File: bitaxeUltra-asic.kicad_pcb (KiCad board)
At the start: 4 copper layers, 56.5 x 99.8 mm, 137 parts, among them J1 54-00164, J2 Conn_01x02, J3 Conn_01x05, J4 Conn_01x04, J5 TC2030-IDC, J7 Conn_01x02, J8 USB_C_Receptacle_USB2.0, J9 Conn_01x04, Q1 CSD17311Q5, Q2 CSD17311Q5, Q4 2N7002K, SW1 GT-TC029B-H025-L1N, SW2 GT-TC029B-H025-L1N, U1 25MHz, U10 DS4432U+, U11 RT9080-33GJ5, U12 ESP32-S3-WROOM-1, U14 BM1366_mode1, U2 TXB0104RGYR, U5 MCP1824T-1802E, U6 MCP1824T-0802E, U7 EMC2101, U8 INA260, U9 TPS40305, Y1 32.768kHz

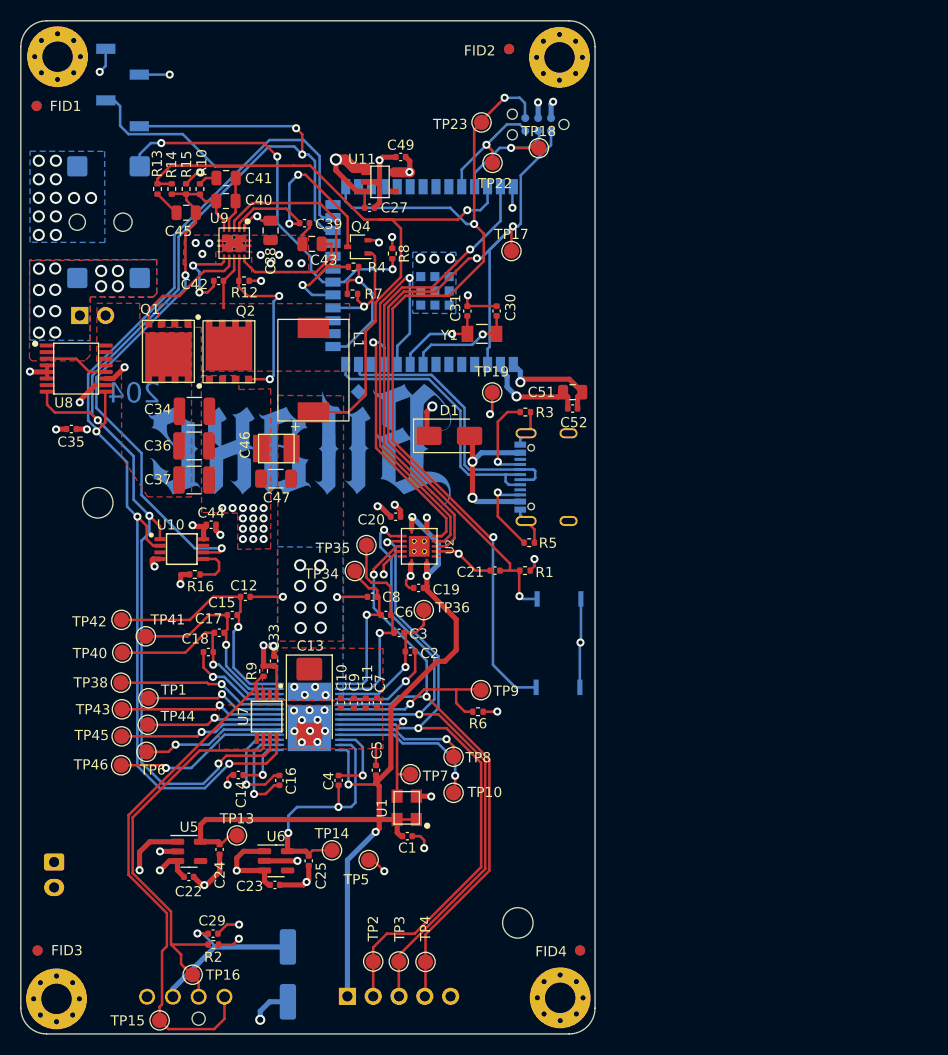
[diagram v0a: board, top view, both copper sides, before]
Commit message: routing for ASIC board
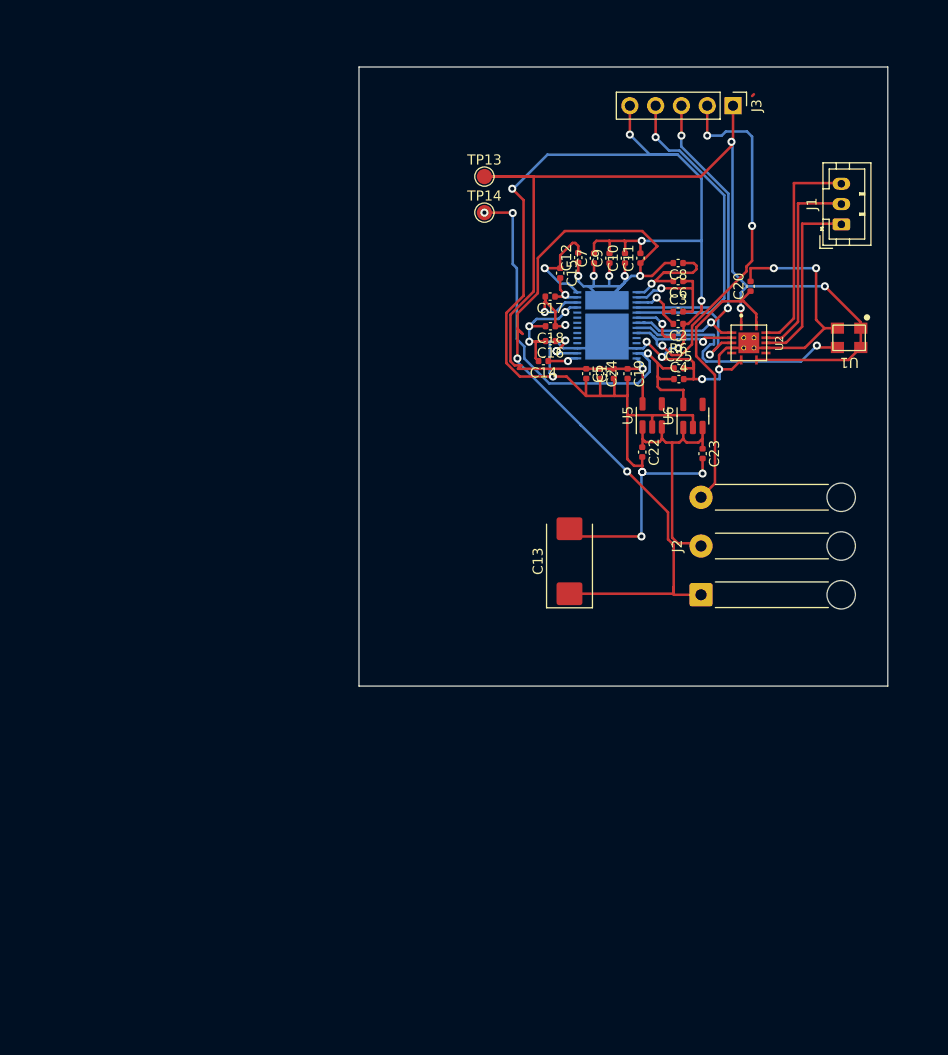
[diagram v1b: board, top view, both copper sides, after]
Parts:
- removed C21, C27, C35, C44, C49: 1uF, Capacitor_SMD:C_0402_1005Metric
- removed C28: 220uF, Capacitor_SMD:CP_Elec_6.3x7.7
- removed C29, C33, C42, C52: 0.1uF, Capacitor_SMD:C_0402_1005Metric
- removed C30, C31: 6.8pF, Capacitor_SMD:C_0402_1005Metric
- removed C34, C36, C37: 47uF, Capacitor_SMD:C_1210_3225Metric
- removed C38: 1uF, Capacitor_SMD:C_0805_2012Metric
- removed C39: 3.3nF, Capacitor_SMD:C_0402_1005Metric
- removed C40: 180pF, Capacitor_SMD:C_0805_2012Metric
- removed C41: 1.5nF, Capacitor_SMD:C_0805_2012Metric
- removed C43, C51: 10uF, Capacitor_SMD:C_0805_2012Metric
- removed C45: 470pF, Capacitor_SMD:C_0805_2012Metric
- removed C46: 220uF, bitaxe:CAP_2R5TPE220MAFB
- removed C47: 100uF, Capacitor_SMD:C_1206_3216Metric
- removed D1: SS310, Diode_SMD:D_SMA
- removed FID1, FID2, FID3, FID4, FID5, FID6, FID7, FID8: Fiducial, Fiducial:Fiducial_1mm_Mask2mm
- removed G***: LOGO, bitaxe:logo
- removed G***: LOGO, bitaxe:logo-fcu
- removed H10, H7, H8, H9: MountingHole_Pad, MountingHole:MountingHole_3mm_Pad_Via
- removed H5, H6: MountingHole, MountingHole:MountingHole_3.5mm
- removed J4: Conn_01x04, bitaxe:470531000
- removed J5: TC2030-IDC, bitaxe:Tag-Connect_TC2030-IDC-NL_2x03_P1.27mm_Vertical
- removed J7: Conn_01x02, Connector_PinHeader_2.54mm:PinHeader_1x02_P2.54mm_Vertical
- removed J8: USB_C_Receptacle_USB2.0, Connector_USB:USB_C_Receptacle_GCT_USB4105-xx-A_16P_TopMnt_Horizontal
- removed J9: Conn_01x04, Connector_PinSocket_2.54mm:PinSocket_1x04_P2.54mm_Vertical_SMD_Pin1Right
- removed L1: 150nH, bitaxe:FP1005R1-R15-R
- removed Q1, Q2: CSD17311Q5, bitaxe:CSD17311Q5
- removed Q4: 2N7002K, Package_TO_SOT_SMD:SOT-323_SC-70
- removed R1, R4, R7, R9: 10k, Resistor_SMD:R_0402_1005Metric
- removed R10: 3.83k, Resistor_SMD:R_0402_1005Metric
- removed R12: 4.12k, Resistor_SMD:R_0402_1005Metric
- removed R13: 1.33k, Resistor_SMD:R_0402_1005Metric
- removed R14: 4.99k, Resistor_SMD:R_0402_1005Metric
- removed R15: 3.32k, Resistor_SMD:R_0402_1005Metric
- removed R16: 80.6k, Resistor_SMD:R_0402_1005Metric
- removed R2: 5.6k, Resistor_SMD:R_0402_1005Metric
- removed R3, R5: 5.1k, Resistor_SMD:R_0402_1005Metric
- removed R8: 1M, Resistor_SMD:R_0402_1005Metric
- removed SW1, SW2: GT-TC029B-H025-L1N, bitaxe:SW_CS1213AGF260_CRS
- removed TP1, TP10, TP15, TP16, TP17, TP18, TP19, TP2, TP22, TP23, TP3, TP34, TP35, TP36, TP38, TP4, TP40, TP41, TP42, TP43, TP44, TP45, TP46, TP5, TP6, TP7, TP8, TP9: TestPoint, TestPoint:TestPoint_Pad_D1.5mm
- removed U10: DS4432U+, Package_SO:TSSOP-8_3x3mm_P0.65mm
- removed U11: RT9080-33GJ5, bitaxe:RT9080-33GJ5
- removed U12: ESP32-S3-WROOM-1, bitaxe:ESP32-S3-WROOM-1
- removed U3: ~, bitaxe:polarity
- removed U7: EMC2101, Package_SO:TSSOP-8_3x3mm_P0.65mm
- removed U8: INA260, Package_SO:TSSOP-16_4.4x5mm_P0.65mm
- removed U9: TPS40305, bitaxe:TPS40305
- removed Y1: 32.768kHz, bitaxe:SC32S-7PF20PPM
- J1: value 54-00164 -> Conn_01x03_Pin; footprint bitaxe:BarrelJack_Wuerth_694106106102_2.0x5.5mm -> Connector_JST:JST_PH_B3B-PH-K_1x03_P2.00mm_Vertical; moved to F.Cu
- J2: value Conn_01x02 -> Conn_01x03_Pin; footprint bitaxe:JST_XH_B2B-XH-A_1x02_P2.50mm_Vertical -> Connector_Wire:SolderWire-0.5sqmm_1x03_P4.8mm_D0.9mm_OD2.3mm_Relief; moved to F.Cu
- J3: moved to F.Cu
- moved J3 95.6 mm to (147.3, 55.9)
- moved J1 72.2 mm to (158.0, 67.6)
- moved TP13 69.3 mm to (122.8, 62.9)
- moved J2 68.9 mm to (144.2, 104.0), turned to 90 degrees
- moved TP14 64.6 mm to (122.8, 66.4)
- moved U1 63.6 mm to (158.8, 78.7), turned to 180 degrees
- moved U5 62.6 mm to (139.4, 86.4), turned to 90 degrees
- moved C22 61.2 mm to (138.4, 90.0), turned to -90 degrees
- moved C25 60.7 mm to (142.0, 81.7), turned to 0 degrees
- moved U6 60.0 mm to (143.4, 86.4), turned to 90 degrees
- moved C24 60.0 mm to (134.2, 82.3)
- moved C23 59.8 mm to (144.3, 90.1), turned to -90 degrees
- moved C10 52.0 mm to (136.7, 70.9), turned to 90 degrees
- moved C4 51.8 mm to (142.0, 82.8), turned to 0 degrees
- moved C11 51.5 mm to (138.2, 70.9), turned to 90 degrees
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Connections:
- J1 pad 1: /Power/VIN -> /RST
- J1 pad 2: GND -> /TX
- J1 pad 3: /PLUG_SENSE -> /RX
- J2 pad 1: GND -> /VDD
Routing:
- net /5V: track 217.6 -> 26.0 mm, vias 7 -> 0
- net /SDA: track 128.0 -> 0.00 mm, vias 5 -> 0
- net /SCL: track 126.5 -> 0.00 mm, vias 3 -> 0
- net /ESP32/IO0: track 92.0 -> 0.00 mm, vias 3 -> 0
- net GND: track 148.3 -> 231.6 mm, vias 83 -> 19
- net /ESP32/EN: track 81.0 -> 0.00 mm, vias 3 -> 0
- net /Power/OUT0: track 55.9 -> 0.00 mm, vias 2 -> 0
- net /Fan/FAN_PWM: track 51.9 -> 0.00 mm
- net /3V3: track 74.3 -> 28.1 mm, vias 15 -> 0
- net /Fan/FAN_TACH: track 40.6 -> 0.00 mm
- net /PLUG_SENSE: track 38.4 -> 0.00 mm, vias 3 -> 0
- net /BM1366/RO: track 66.2 -> 34.8 mm, vias 2 -> 3
- net /RST: track 46.2 -> 18.2 mm, vias 1 -> 0
- net Net-(U12-GPIO20/U1CTS/ADC2_CH9/CLK_OUT1/USB_D+): track 27.8 -> 0.00 mm
- net Net-(U12-GPIO19/U1RTS/ADC2_CH8/CLK_OUT2/USB_D-): track 27.5 -> 0.00 mm
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- removed copper zone on In2.Cu, net /3V3
- removed copper zone on F.Cu, net /5V
- removed copper zone on F.Cu, net /Power/SW
- removed copper zone on B.Cu, net /Power/VIN
- removed copper zone on F.Cu, net /Power/VIN
- removed copper zone on B.Cu, net /VDD
- removed copper zone on F.Cu, net /VDD
- removed copper zone on B.Cu, net GND
- removed copper zone on F.Cu, net GND
- removed copper zone on In1.Cu, net GND
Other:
- board size 56.5 x 99.8 mm -> 52.1 x 61 mm
- board text removed: "/ 21M"
- board text removed: "1V8"
- board text removed: "204"
- board text removed: "5V"
- board text removed: "GND"
- board text removed: "PWM"
- board text removed: "RST"
- board text removed: "RXI"
- board text removed: "TAC"
- board text removed: "TXO"
- board text removed: "∞"

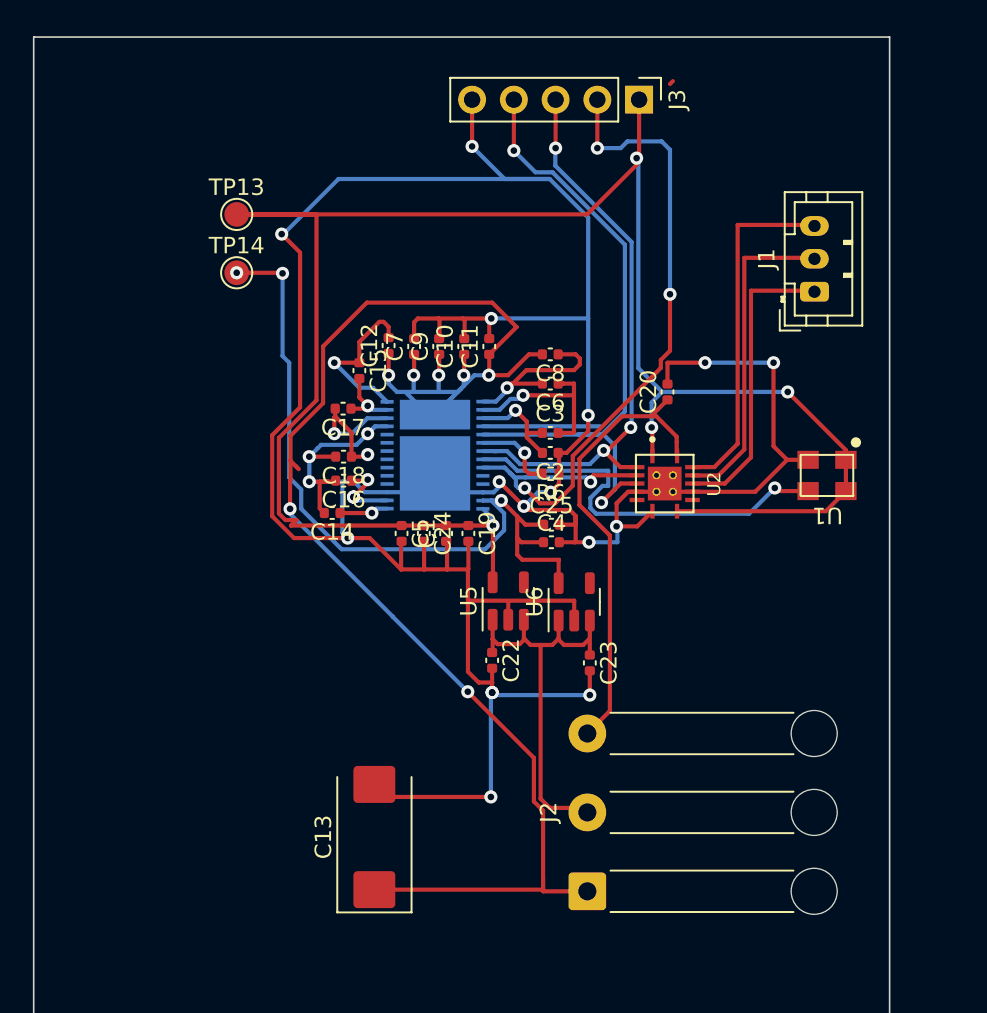
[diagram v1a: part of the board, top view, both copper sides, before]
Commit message: revert  to 4 layer-board routing
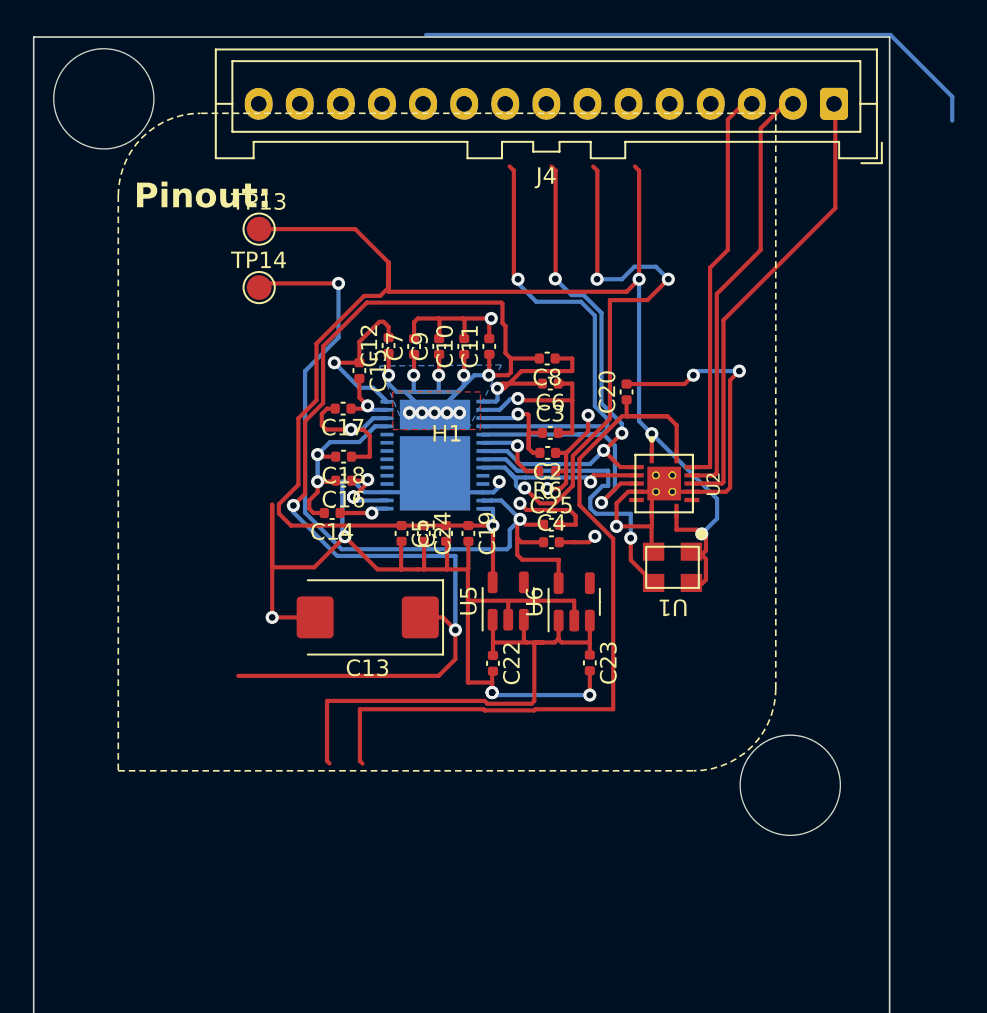
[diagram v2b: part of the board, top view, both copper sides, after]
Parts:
- removed J1: Conn_01x03_Pin, Connector_JST:JST_PH_B3B-PH-K_1x03_P2.00mm_Vertical
- removed J2: Conn_01x03_Pin, Connector_Wire:SolderWire-0.5sqmm_1x03_P4.8mm_D0.9mm_OD2.3mm_Relief
- removed J3: Conn_01x05, Connector_PinHeader_2.54mm:PinHeader_1x05_P2.54mm_Vertical
- added H1: MountingHole, bitaxe:heatsink_mount_bridge, F.Cu at (135.6, 76.7)
- added J4: Conn_01x15, Connector_JST:JST_XA_B15B-XASK-1_1x15_P2.50mm_Vertical, F.Cu at (159.2, 56.1)
- moved C13 13.4 mm to (130.8, 87.4), turned to 180 degrees
- moved U1 10.9 mm to (149.4, 84.3)
- moved C20 2.49 mm to (146.6, 73.7)
- moved TP14 1.64 mm to (124.2, 67.3)
- moved TP13 1.63 mm to (124.2, 63.8)
- moved C8 0.31 mm to (141.7, 71.6)
- moved R6 0.26 mm to (141.7, 78.5)
- moved C22 0.19 mm to (138.4, 90.2)
- moved C2 0.16 mm to (141.8, 77.4)
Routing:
- net GND: track 231.6 -> 157.8 mm, vias 19 -> 16
- net (no net): track 0.00 -> 35.0 mm
- net /BM1366/1V8: track 117.3 -> 96.8 mm
- net /3V3: track 28.1 -> 47.5 mm
- net /RST: track 18.2 -> 28.3 mm
- net /VDD: track 98.1 -> 88.1 mm, vias 7 -> 12
- net /5V: track 26.0 -> 33.8 mm
- net /BM1366/CLKI: track 25.0 -> 18.2 mm
- net /TX: track 19.8 -> 26.5 mm
- net /BM1366/RO: track 34.8 -> 30.6 mm
- net /BM1366/RST_N: track 40.5 -> 36.6 mm
- net /RX: track 21.4 -> 24.8 mm
- net /BM1366/CI: track 46.1 -> 43.6 mm
- net /BM1366/VDD3_0: track 6.39 -> 7.66 mm
- net /BM1366/0V8: track 46.0 -> 46.9 mm, vias 3 -> 2
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- added copper zone on B.Cu, net /VDD
- added copper zone on F.Cu, net /VDD
- added copper zone on In2.Cu, net /VDD
- added copper zone on In1.Cu, net GND
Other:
- board text added: "Pinout:"
